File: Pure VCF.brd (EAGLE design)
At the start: 33.6 x 100 mm, 82 parts, among them T1 TRANS_PAIR_PNP, U1 QUAD_OPAMP, U2 LM13700, U3 DUAL_OPAMP, U4 LM13700

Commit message: VCF 2.2
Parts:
- added U$1, U$2: (no value), gmsnLogo:GMSN!_LOGO
- C10, C11, C12, C9: value 100nF -> 0.1u; device rcl:C1206K -> rcl:C0805K
- C14, C15, C16, C17: value * -> 0.1u
- R21: value 300K -> 75K***
- R22: value 49K9 -> 1M***
- R23: value 100K -> 4k12
- R3: value 100K -> 1M***
- R39: value 2K2 -> 4k12
- R4: value 100K -> 1M5***
- R6: value 220K -> 2M***
- R7: value 2K2 -> 0R***
- TR1: value 100R -> 100K; device INSTRUO:TRIM_3269W -> INSTRUO:TRIMMER_TH3
- TR2: value 100R -> 100k
- moved R21 67.3 mm to (28.3, 40.2), flipped to the top, turned to 0 degrees
- moved R22 39.4 mm to (22.4, 65.9), flipped to the top, turned to 0 degrees
- moved C16 31.0 mm to (2.30, 65.6), flipped to the top
- moved R37 30.0 mm to (2.78, 39.1), flipped to the top
- moved R17 29.8 mm to (32.7, 74.3), flipped to the top
- moved R23 29.5 mm to (3.02, 106.5), flipped to the top
- moved R10 29.4 mm to (3.10, 86.4), flipped to the top
- moved R35 29.4 mm to (32.5, 61.8), flipped to the top
- moved C9 29.2 mm to (32.4, 56.5), flipped to the top
- moved D2 28.3 mm to (3.65, 21.9), flipped to the top
- moved R38 28.3 mm to (3.65, 42.9), flipped to the top
- moved R39 28.1 mm to (3.73, 53.9), flipped to the top
- moved C13 26.7 mm to (4.45, 48.6), flipped to the top
- moved C8 26.7 mm to (4.45, 71.0), flipped to the top
- moved C7 26.4 mm to (31.0, 65.9), flipped to the top
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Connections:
- net -12V: now also R21.1; no longer COF.P$1
- net GND: now also R22.2; no longer U1.1+IN
- net N$19: now also R23.1; no longer R22.1
- net N$20: now also Q.P$3, U1.1OUT; no longer R21.1, R22.2
- net N$25: now also COF.P$1; no longer R23.1, U1.1OUT
- net N$46: now also U1.1+IN; no longer Q.P$3
- net N$7: now also R22.1
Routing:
- net N$20: track 10.4 -> 129.9 mm, vias 0 -> 1
- net N$46: track 77.9 -> 125.9 mm, vias 2 -> 4
- net N$19: track 103.0 -> 114.6 mm
- net N$25: track 12.9 -> 3.24 mm
- net N$5: track 11.9 -> 15.8 mm
- net N$2: track 10.4 -> 14.0 mm
- net +12V: track 206.1 -> 209.2 mm
- net N$7: track 34.3 -> 36.5 mm
- net N$3: track 4.21 -> 2.18 mm
- net N$56: track 0.00 -> 1.91 mm
- net -12V: track 243.7 -> 241.8 mm, vias 10 -> 11
- net N$8: track 79.1 -> 80.9 mm
- net GND: track 10.3 -> 8.48 mm, vias 16 -> 18
- net N$44: track 23.4 -> 25.1 mm
- net N$40: track 28.6 -> 27.8 mm
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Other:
- board text added: "Pure VCF V2.2"
- board text added: "copyright GMSN Ltd 2016"

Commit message: VCF 2.3
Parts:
- removed R22: 1M***, rcl:R0805
- removed R5: 220K, rcl:R0805
- removed U1: QUAD_OPAMP, INSTRUO:QUAD_OPAMP
- removed U2, U4: LM13700, INSTRUO:SOIC-16_BLANK
- removed U3: DUAL_OPAMP, INSTRUO:DUAL_OPAMP
- added IC4, IC5: TL074D, GMSN:SO14
- added U$3, U$4: LM13700, GMSN:SOIC-16_BLANK
- 2POLE, 4POLE, COF_CV: value (none) -> S_JACK; device INSTRUO:S_JACK -> GMSN:S_JACK
- C13, C8: device rcl:153CLV-0505 -> GMSN:153CLV-0505
- C3: device rcl:C0805K -> GMSN:C0805K
- C4, C5, C6, C7: device rcl:C0805K -> rcl:C050-045X075
- COF, CV_AT, IN1POT, IN1POT1: device INSTRUO:Q-POT -> GMSN:POT
- Q: value 100K -> 100k; device INSTRUO:Q-POT -> GMSN:POT
- R0: value 2K -> 2k
- R1, R10, R13, R15, R18, R26, R30, R31, R34, R41, R43, R44, R8: value 100K -> 100k; device rcl:R0805 -> GMSN:R0805
- R11, R20, R28, R42: value 33K -> 33k; device rcl:R0805 -> GMSN:R0805
- R12, R16, R17, R2, R27, R29, R33, R36, R6, R9: device rcl:R0805 -> GMSN:R0805
- R14, R32, R35: value 10K -> 10k; device rcl:R0805 -> GMSN:R0805
- R19: value 100K -> 10k; device rcl:R0805 -> GMSN:R0805
- R21: value 75K*** -> 75k
- R23: value 4k12 -> 10k; device rcl:R0805 -> GMSN:R0805
- R24, R25, R37, R38, R40: value 2K2 -> 100k; device rcl:R0805 -> GMSN:R0805
- R3: value 1M*** -> 100k; device rcl:R0805 -> GMSN:R0805
- R39: value 4k12 -> 100k; device rcl:R0805 -> GMSN:R0805
- R4: value 1M5*** -> 100k; device rcl:R0805 -> GMSN:R0805
- R7: value 0R*** -> 2k2; device rcl:R0805 -> GMSN:R0805
- T1: device INSTRUO:TRANS_PAIR -> GMSN:TRANS_PAIR
- TR1: value 100K -> 100k; device INSTRUO:TRIMMER_TH3 -> GMSN:TRIMMER_TH3
- TR2: value 100k -> TRIMMER_TH3; device INSTRUO:TRIM_3269W -> GMSN:TRIMMER_TH3
- moved R23 82.9 mm to (26.0, 26.9), turned to 90 degrees
- moved C9 48.6 mm to (18.7, 103.2), turned to 0 degrees
- moved U$2 37.0 mm to (8.97, 114.8), turned to 0 degrees
- moved C10 34.2 mm to (15.4, 53.9), turned to 180 degrees
- moved C14 29.2 mm to (14.9, 74.0), turned to 180 degrees
- moved TR2 26.4 mm to (31.5, 77.1), turned to 270 degrees
- moved C8 25.7 mm to (6.67, 45.4), turned to 180 degrees
- moved C15 25.3 mm to (3.33, 112.8), turned to 0 degrees
- moved R10 24.9 mm to (26.5, 77.8), turned to 0 degrees
- moved C16 24.7 mm to (11.7, 42.7), turned to 180 degrees
- moved D2 22.9 mm to (26.4, 19.5), turned to 180 degrees
- moved R33 20.3 mm to (26.8, 60.2), turned to 0 degrees
- moved R36 20.2 mm to (23.3, 55.9)
- moved R40 19.8 mm to (12.7, 46.7), turned to 90 degrees
- moved R7 19.3 mm to (14.4, 95.6)
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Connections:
- removed net N$34: R29.1, R30.1, U4.4
- removed net N$42: R41.2, R43.1, R44.1, U1.2-IN
- removed net N$45: C7.1, U4.10, U4.12
- removed net N$48: R42.1, U4.16
- removed net N$51: U4.2
- removed net N$52: U4.15
- new net N$57: C6.1, U$4.5, U$4.7
- new net N$58: C7.1, U$4.10, U$4.12
- new net N$59: R28.1, U$4.1
- net +12V: now also IC4.4, IC5.4, U$3.11, U$4.11; no longer U1.VCC++, U2.11, U3.+VCC, U4.11
- net -12V: now also IC4.11, IC5.11, U$3.6, U$4.6; no longer U1.VCC--, U2.6, U3.-VCC, U4.6
- net GND: now also IC4.10, IC4.3, IC4.5, IC5.12, IC5.3, IC5.5; no longer R22.2, R5.1, U1.2+IN, U3.+1IN, U3.+2IN
- net N$1: now also C5.1, U$3.10, U$3.12; no longer U2.2
- net N$11: now also IC4.2; no longer U1.4-IN
- net N$12: now also IC4.1; no longer U1.4OUT
- net N$13: now also U$3.1; no longer U2.1
- net N$15: now also IC4.6, R41.2, R43.1, R44.1; no longer R5.2, U1.4+IN
- net N$16: now also U$3.9; no longer U2.9
- net N$17: now also U$3.3; no longer U2.3
- net N$18: now also C8.-, IC5.2, R40.1; no longer R10.1, R12.1, R13.1, R23.2, U2.4
- net N$20: now also IC5.8, IC5.9; no longer U1.1-IN, U1.1OUT
- net N$21: now also C13.-, IC5.6, R39.1; no longer C8.-, R40.1, U3.-2IN
- net N$22: now also U$3.16; no longer U2.16
- net N$23: now also U$3.14; no longer U2.14
- net N$24: now also U$3.13; no longer U2.13
- net N$27: now also U$3.5, U$3.7; no longer U2.5, U2.7
- net N$28: now also U$3.8; no longer U2.8
- net N$29: now also R26.1, R27.1, U$4.3; no longer C5.1, U2.10, U2.12
- net N$30: now also IC5.1; no longer U3.2OUT
- net N$31: now also R42.1, U$4.16; no longer R28.1, U4.1
- net N$32: now also IC4.7; no longer U1.2OUT
- net N$33: now also R29.1, R30.1, U$4.4; no longer R26.1, R27.1, U4.3
- net N$37: now also IC5.13, IC5.14; no longer C13.-, R39.1, U3.-1IN
- net N$39: now also IC4.8, IC4.9; no longer R31.1, R33.1, U4.14
- net N$4: now also R10.1, R12.1, R13.1, R23.2, U$3.4; no longer U2.15
- net N$40: now also U$4.13; no longer U4.13
- net N$41: now also IC5.7; no longer U3.1OUT
- net N$43: now also R31.1, R33.1, U$4.14; no longer C6.1, U4.5, U4.7
- net N$44: now also U$4.8; no longer U4.8
- net N$46: now also IC5.10, U$4.9; no longer U1.1+IN, U4.9
- net N$5: now also IC4.14; no longer U1.3OUT
- net N$6: now also IC4.13; no longer U1.3-IN
- net N$7: no longer R22.1
- net N$8: now also IC4.12; no longer U1.3+IN
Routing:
- net N$19: track 114.6 -> 2.71 mm, vias 1 -> 0
- net N$4: track 0.00 -> 110.3 mm, vias 0 -> 3
- net N$20: track 129.9 -> 21.5 mm
- net N$46: track 125.9 -> 38.4 mm, vias 4 -> 2
- net N$42: track 84.5 -> 0.00 mm
- net +12V: track 209.2 -> 161.8 mm, vias 8 -> 5
- net N$15: track 3.61 -> 47.7 mm
- net N$44: track 25.1 -> 59.4 mm, vias 2 -> 0
- net N$39: track 30.7 -> 1.27 mm
- net N$32: track 8.83 -> 35.6 mm, vias 0 -> 2
- net N$18: track 32.4 -> 8.22 mm
- net N$7: track 36.5 -> 13.0 mm
- net N$49: track 36.4 -> 13.9 mm
- net N$34: track 20.7 -> 0.00 mm
- net N$5: track 15.8 -> 35.3 mm
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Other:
- board text added: "Pure VCF V2.3"
- board text removed: "-12V"
- board text removed: "Pure VCF V2.2"
- board text removed: "TR1"
- board text removed: "TR2"

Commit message: VCF 2.4
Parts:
- removed R0: 2k, INSTRUO:RESISTOR_TC
- added R5: Tempco 2k, GMSN:0204/7
- 2POLE, 4POLE, COF_CV: value S_JACK -> PJ301M-12; device GMSN:S_JACK -> GMSN:PJ301M-12
- C1, C2: value 10u -> 10uF; device rcl:153CLV-0505 -> GMSN:153CLV-0505
- C10, C11, C12, C14, C15, C16, C17, C9: value 0.1u -> 100nF; device rcl:C0805K -> GMSN:C0805
- C13, C8: value 10u -> 10uF
- C3: value 20pF -> 22pF; device GMSN:C0805K -> GMSN:C0805
- C4, C5, C6, C7: device rcl:C050-045X075 -> GMSN:C050-045X075
- COF, CV_AT, IN1POT, IN1POT1: value 100K -> 100k; device GMSN:POT -> GMSN:POTENTIOMETER_9MM
- D1, D2: value (none) -> STTH102A; device adafruit:SMADIODE -> GMSN:SMADIODE
- IC3, IC4: value TL074D -> TL074
- IN1, IN2: value (none) -> PJ301M-12; device INSTRUO:S_JACK -> GMSN:PJ301M-12
- JP1: value M05X2SHD -> HEADER2X5SHD; device SparkFun-Connectors:2X5-SHROUDED -> GMSN:2X5-SHROUDED
- Q: device GMSN:POT -> GMSN:POTENTIOMETER_9MM
- R21: device rcl:R0805 -> GMSN:R0805
- R6: value 2M*** -> 2M
- T1: value TRANS_PAIR_PNP -> DMMT3906W
- TR1: device GMSN:TRIMMER_TH3 -> GMSN:TRIMMER_TH
- TR2: value TRIMMER_TH3 -> 100k; device GMSN:TRIMMER_TH3 -> GMSN:TRIMMER_TH
- moved JP1 1.84 mm to (17.1, 27.0)
- moved R30 1.27 mm to (5.71, 57.5)
- moved R25 0.93 mm to (3.33, 52.8)
- turned U$1 to 0 degrees
- renumbered IC5 to IC3, R44 to R22, U$3 to IC1, U$4 to IC2
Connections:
- net N$5: now also R5.2; no longer R0.2
- net N$6: now also R5.1; no longer R0.1
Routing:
- net N$5: track 35.3 -> 41.0 mm
- net N$3: track 2.87 -> 6.36 mm
- net N$20: track 21.5 -> 18.4 mm
- net N$2: track 11.1 -> 14.0 mm
- net N$50: track 16.0 -> 18.8 mm
- net +12V: track 161.8 -> 164.1 mm
- net N$54: track 4.35 -> 6.58 mm
- net N$46: track 38.4 -> 39.4 mm
- net N$44: track 59.4 -> 60.4 mm
- net N$26: track 24.5 -> 25.4 mm
- net N$38: track 13.2 -> 12.3 mm
- net N$33: track 10.6 -> 9.89 mm
- net N$6: track 22.7 -> 23.2 mm
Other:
- board text added: "Pure VCF V2.4"
- board text added: "cc-by 4.0"
- board text removed: "Pure VCF V2.3"
- board text removed: "copyright GMSN Ltd 2016"

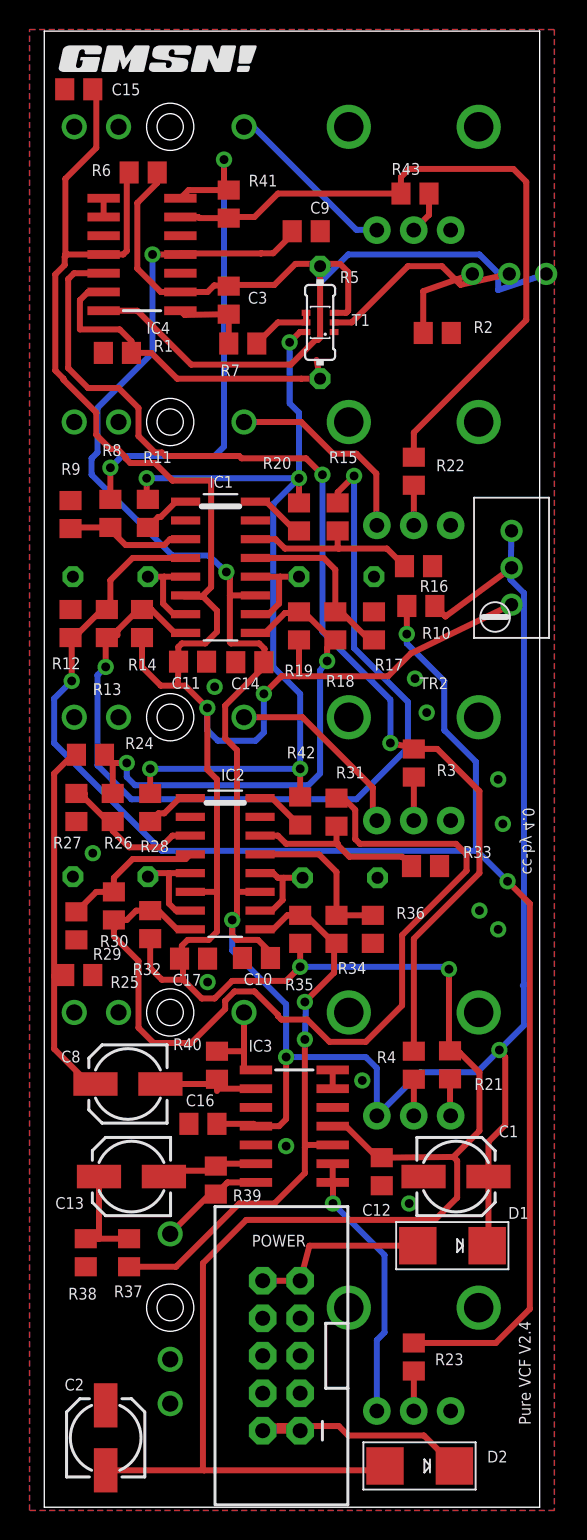
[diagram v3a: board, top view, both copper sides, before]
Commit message: VCF 2.5 beta
VCF Updated to V2.5 14/04/21

Library updated to 3D models.
Changed the CV mixer from Average to Sum and added inverter stage to retain consistency.
Some resistor values reduced to 10K, inline with low noise techniques.
Rerouted and reduced some traces.
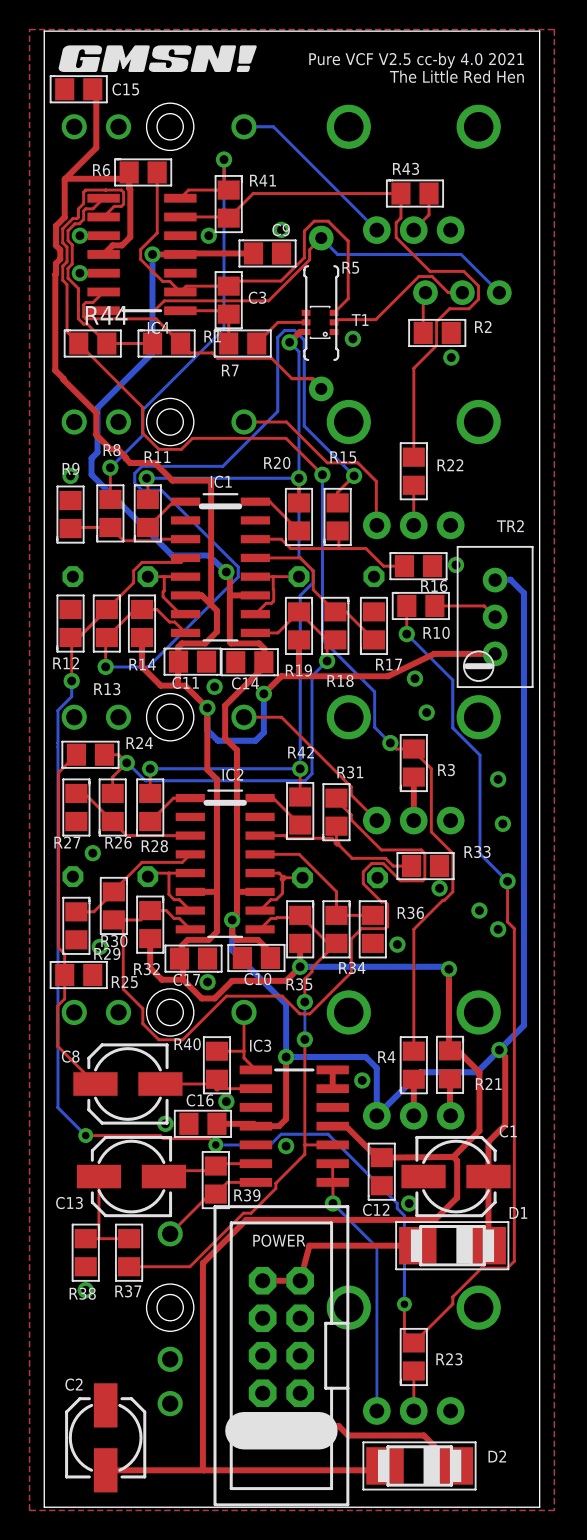
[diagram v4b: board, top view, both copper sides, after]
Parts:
- added R44: 10k, GMSN:R0805
- COF: value 100k -> 10k; device GMSN:POTENTIOMETER_9MM -> GMSN:POT_9MM_RED_KNOB
- CV_AT: value 100k -> 10k; device GMSN:POTENTIOMETER_9MM -> GMSN:POT_9MM_GREEN_KNOB
- IN1POT, IN1POT1: value 100k -> 10k; device GMSN:POTENTIOMETER_9MM -> GMSN:POT_9MM_BLUE_KNOB
- Q: value 100k -> 10k; device GMSN:POTENTIOMETER_9MM -> GMSN:POT_9MM_YELLOW_KNOB
- R1, R22, R24, R25, R3, R37, R38, R39, R4, R40, R41, R43: value 100k -> 10k
- R5: device GMSN:0204/7 -> GMSN:0207/8.5
- moved TR2 3.51 mm to (30.4, 73.7)
- moved TR1 3.42 mm to (26.0, 97.9)
- moved R1 3.39 mm to (9.29, 95.6)
- moved C9 3.02 mm to (16.1, 101.7)
- moved U$1 1.86 mm to (10.6, 100.2)
- moved R5 0.64 mm to (19.8, 97.6)
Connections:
- removed net N$8: IC4.12, R3.2, R4.2
- new net N$34: IC4.8, R1.1, R44.2
- net GND: now also IC4.12, T1.1; no longer R1.1, T1.B2
- net N$11: now also T1.3; no longer T1.C1
- net N$14: now also T1.4, T1.5; no longer T1.E1, T1.E2
- net N$2: now also T1.2; no longer T1.B1
- net N$35: now also T1.6; no longer T1.C2
- net N$39: now also R3.2, R4.2, R44.1; no longer IC4.8
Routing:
- net N$39: track 1.27 -> 83.4 mm, vias 0 -> 2
- net N$8: track 76.8 -> 0.00 mm, vias 2 -> 0
- net N$4: track 110.3 -> 139.0 mm, vias 3 -> 6
- net N$34: track 0.00 -> 15.9 mm
- net N$5: track 41.0 -> 30.8 mm
- net N$15: track 47.7 -> 39.9 mm
- net +12V: track 164.1 -> 158.3 mm
- net N$44: track 60.4 -> 55.1 mm
- net N$32: track 35.6 -> 31.9 mm
- net N$2: track 14.0 -> 10.4 mm
- net N$3: track 6.36 -> 2.79 mm
- net N$11: track 26.7 -> 30.2 mm
- net N$54: track 6.58 -> 4.39 mm
- net N$50: track 18.8 -> 17.0 mm
- net N$29: track 10.1 -> 8.90 mm
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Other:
- board text added: "Pure VCF V2.5 cc-by 4.0 2021 The Little Red Hen"
- board text removed: "Pure VCF V2.4"
- board text removed: "cc-by 4.0"
